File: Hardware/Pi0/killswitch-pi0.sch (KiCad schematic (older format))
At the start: 29 parts, among them J1 PWR_IN, J2 REMOTE, J3 PI, Q1 Q_PMOS_GSD, SW1 SW_Push, U1 ATTINY84-20SSU, U2 TSDP341xx, U3 AZ1117-3.3, U4 TXB0108DQSR

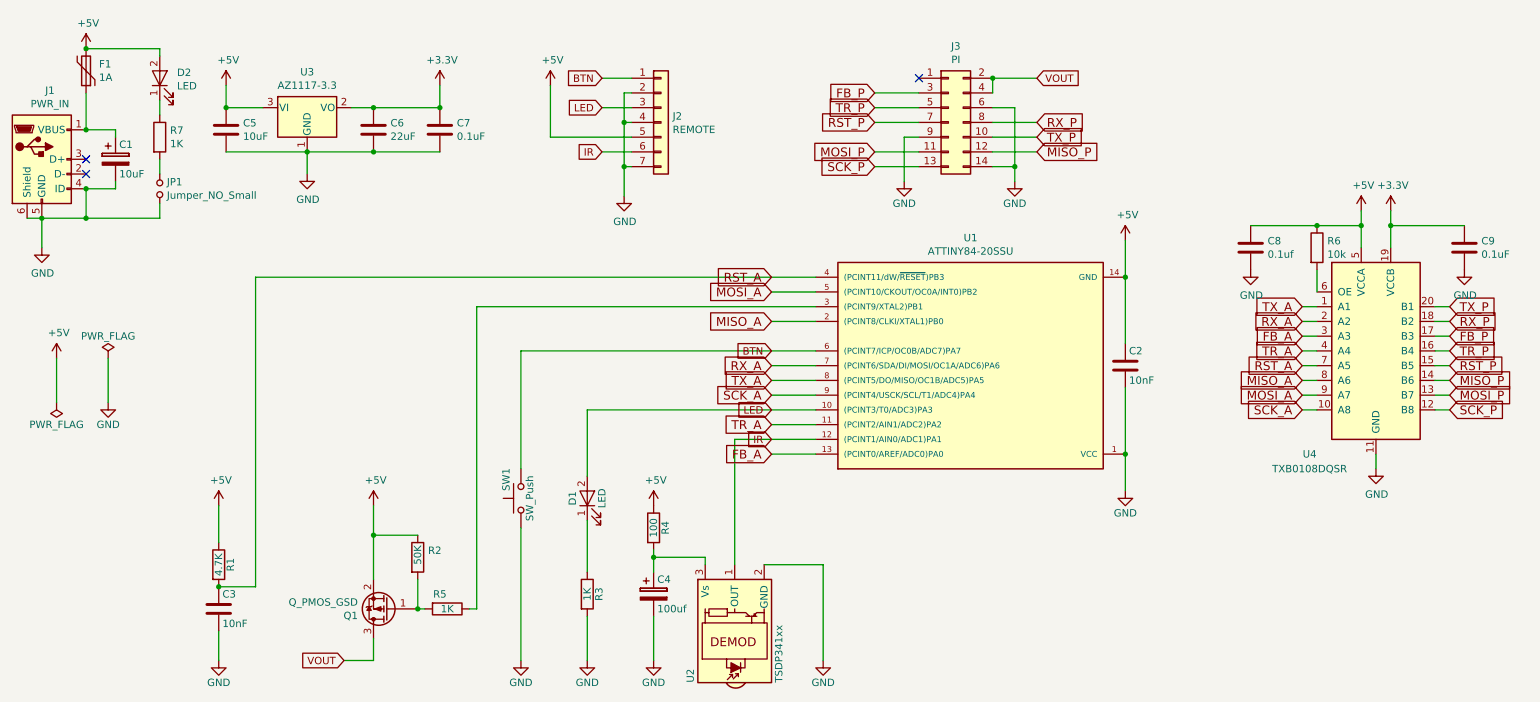
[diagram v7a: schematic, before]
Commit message: Clean up schematic/remove level shifter
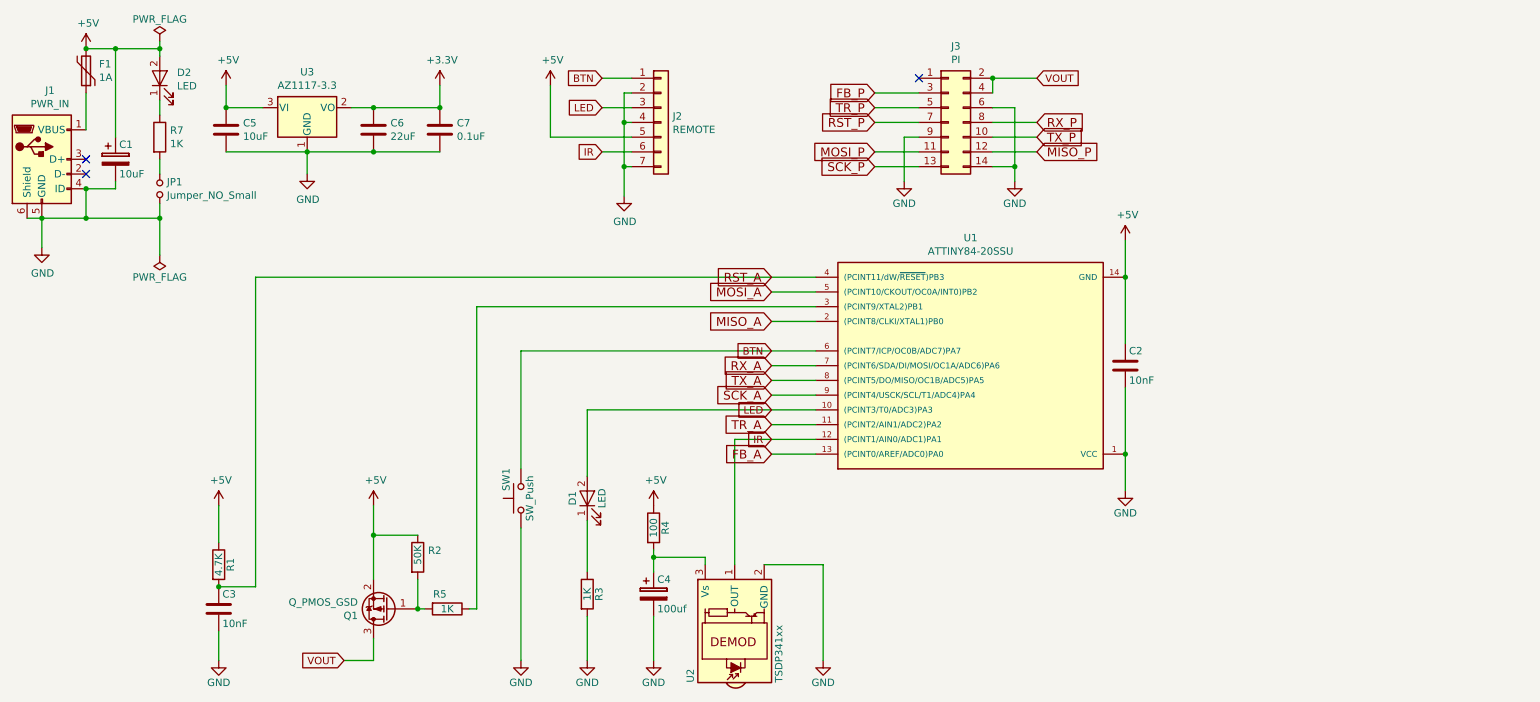
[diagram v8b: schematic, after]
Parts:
- removed C8: 0.1uf, Capacitors_SMD:C_0603_HandSoldering, symbol device:C
- removed C9: 0.1uF, Capacitors_SMD:C_0603_HandSoldering, symbol device:C
- removed R6: 10k, Resistors_SMD:R_0603_HandSoldering, symbol device:R
- removed U4: TXB0108DQSR, Housings_SON:USON-20_2x4mm_Pitch0.4mm, symbol texas:TXB0108DQSR
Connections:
- net +5V: now also C1.1
- net at F1.1, J1.1 (VBUS): no longer C1.1
